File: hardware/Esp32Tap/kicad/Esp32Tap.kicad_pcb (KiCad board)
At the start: 2 copper layers, 100 x 55 mm, 53 parts, among them J1 RJ45_Console_54602-908LF, J2 RJ45_Motor_54602-908LF, J3 USB-C_HRO_TYPE-C-31-M-12, K1 G6K-2F-Y-TR DC3, Q1 S8050, SW1 KMR2-EN, SW2 KMR2-BOOT, U1 ESP32-S3-WROOM-1-N8, U2 TPS54202DDCR, U3 USBLC6-2SC6

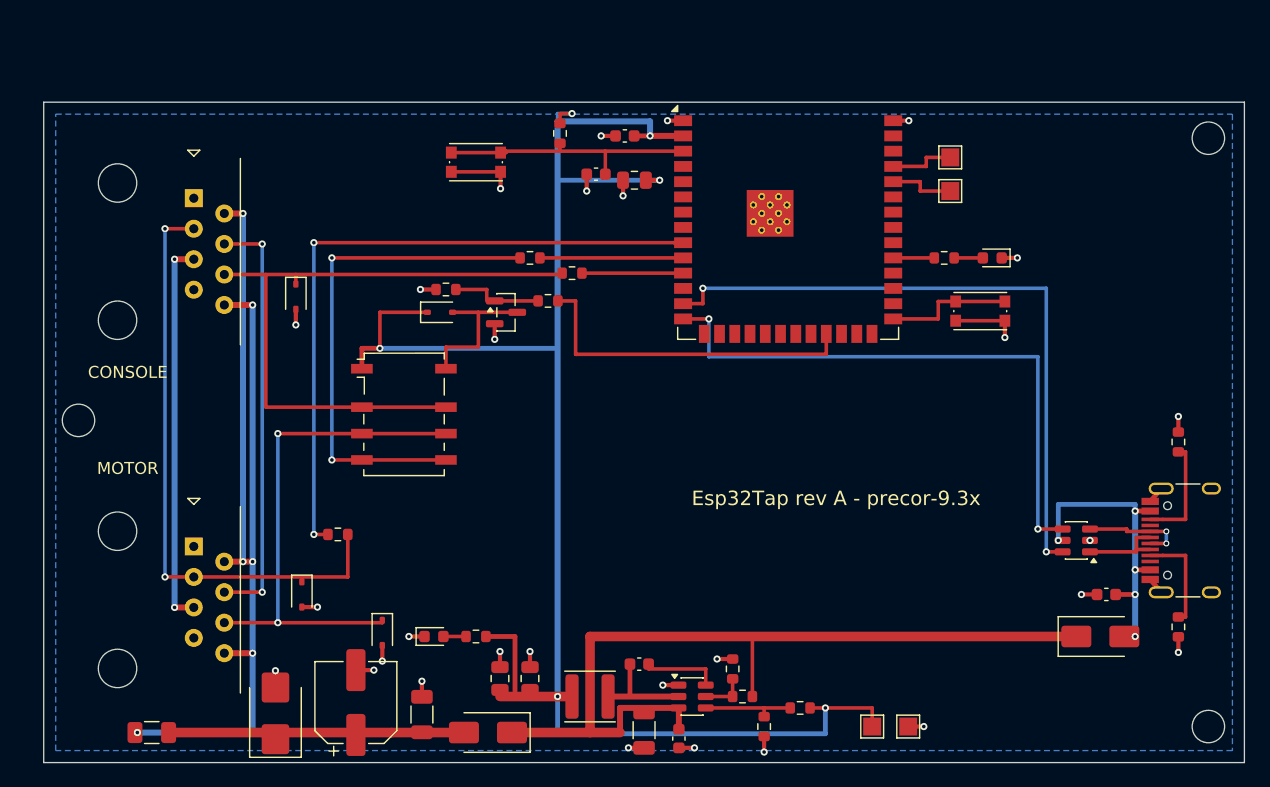
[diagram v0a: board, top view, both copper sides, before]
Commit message: hardware: generate validated Esp32Tap Rev B PCB
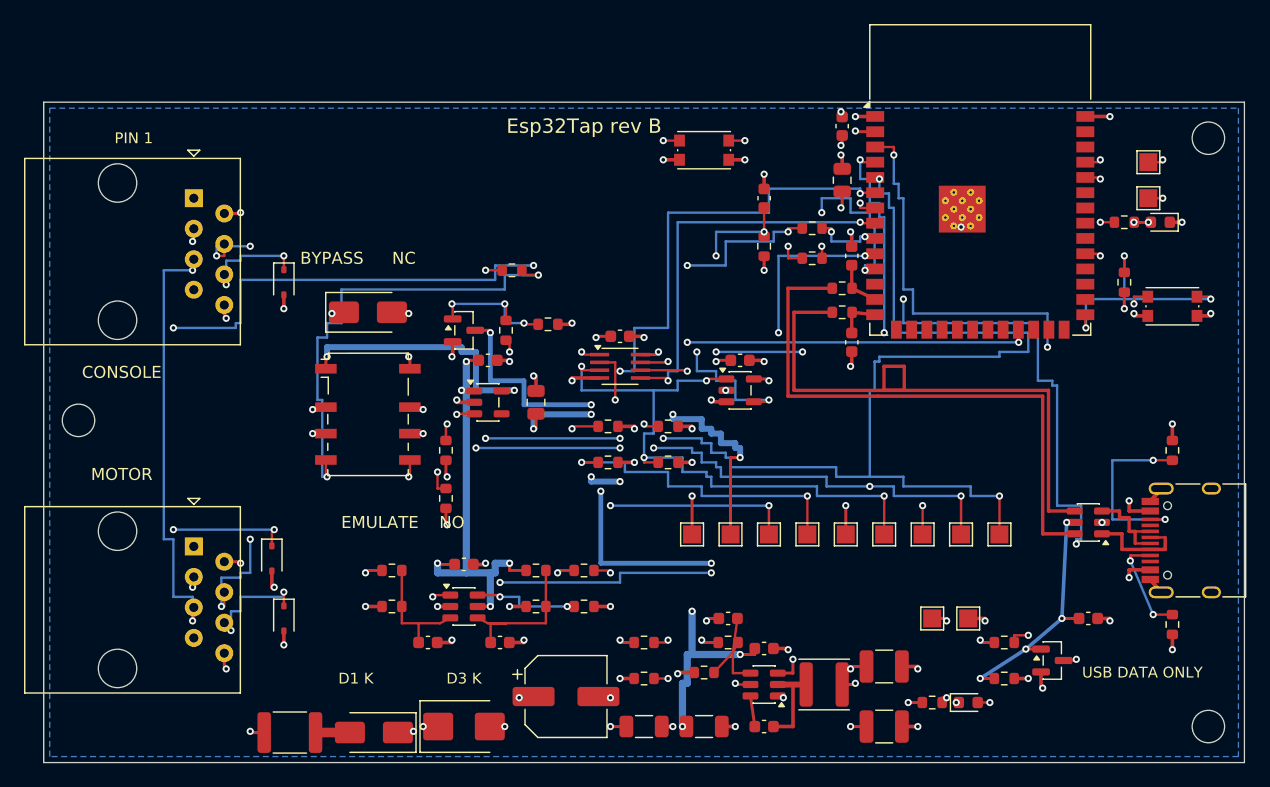
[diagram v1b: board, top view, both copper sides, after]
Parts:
- removed D2: SS34, D_SMA
- added C12: 56pF C0G 0603, Capacitor_SMD:C_0603_1608Metric, F.Cu at (157.0, 143.0)
- added C13: DNP, Capacitor_SMD:C_0603_1608Metric, F.Cu at (167.3, 112.8)
- added C14: DNP, Capacitor_SMD:C_0603_1608Metric, F.Cu at (167.3, 120.0)
- added C15: 1uF/25V X7R 0603, Capacitor_SMD:C_0603_1608Metric, F.Cu at (137.0, 121.5)
- added C16: 4.7uF/25V X7R 0805, Capacitor_SMD:C_0805_2012Metric, F.Cu at (141.0, 125.0)
- added C17: 100nF, Capacitor_SMD:C_0603_1608Metric, F.Cu at (135.0, 138.5)
- added C18: 1nF/50V C0G 0603, Capacitor_SMD:C_0603_1608Metric, F.Cu at (132.0, 145.0)
- added C19: 1nF/50V C0G 0603, Capacitor_SMD:C_0603_1608Metric, F.Cu at (138.0, 145.0)
- added C20: 100nF, Capacitor_SMD:C_0603_1608Metric, F.Cu at (148.0, 119.5)
- added C21: 100nF, Capacitor_SMD:C_0603_1608Metric, F.Cu at (158.0, 121.5)
- added Q2: 2N7002, Package_TO_SOT_SMD:SOT-23, F.Cu at (184.0, 146.5)
- added R15: 22R, Resistor_SMD:R_0603_1608Metric, F.Cu at (166.5, 115.5)
- added R16: 22R, Resistor_SMD:R_0603_1608Metric, F.Cu at (166.5, 117.5)
- added R17: 150k, Resistor_SMD:R_0603_1608Metric, F.Cu at (129.0, 139.0)
- added R18: 10k, Resistor_SMD:R_0603_1608Metric, F.Cu at (129.0, 142.0)
- added R19: 255k, Resistor_SMD:R_0603_1608Metric, F.Cu at (141.0, 139.0)
- added R20: 10k, Resistor_SMD:R_0603_1608Metric, F.Cu at (141.0, 142.0)
- added R21: 10k, Resistor_SMD:R_0603_1608Metric, F.Cu at (145.0, 139.0)
- added R22: 100k, Resistor_SMD:R_0603_1608Metric, F.Cu at (145.0, 142.0)
- added R23: 10k, Resistor_SMD:R_0603_1608Metric, F.Cu at (147.0, 127.0)
- added R24: 10k, Resistor_SMD:R_0603_1608Metric, F.Cu at (147.0, 130.0)
- added R25: 10k, Resistor_SMD:R_0603_1608Metric, F.Cu at (133.5, 129.0)
- added R26: 10k, Resistor_SMD:R_0603_1608Metric, F.Cu at (133.5, 133.0)
- added R27: 10k, Resistor_SMD:R_0603_1608Metric, F.Cu at (152.0, 127.0)
- added R28: 10k, Resistor_SMD:R_0603_1608Metric, F.Cu at (152.0, 130.0)
- added R29: 10k, Resistor_SMD:R_0603_1608Metric, F.Cu at (180.0, 148.0)
- added R30: 10k, Resistor_SMD:R_0603_1608Metric, F.Cu at (180.0, 145.0)
- added R31: 10k, Resistor_SMD:R_0603_1608Metric, F.Cu at (190.0, 115.0)
- added TP10: TX_GATE, TestPoint:TestPoint_Pad_1.5x1.5mm, F.Cu at (170.0, 136.0)
- added TP11: TX_DRV, TestPoint:TestPoint_Pad_1.5x1.5mm, F.Cu at (173.2, 136.0)
- added TP12: K1_NC_FB, TestPoint:TestPoint_Pad_1.5x1.5mm, F.Cu at (176.4, 136.0)
- added TP13: K1_NO_FB, TestPoint:TestPoint_Pad_1.5x1.5mm, F.Cu at (179.6, 136.0)
- added TP5: VIN, TestPoint:TestPoint_Pad_1.5x1.5mm, F.Cu at (154.0, 136.0)
- added TP6: +5V_RLY, TestPoint:TestPoint_Pad_1.5x1.5mm, F.Cu at (157.2, 136.0)
- added TP7: TREAD_OK, TestPoint:TestPoint_Pad_1.5x1.5mm, F.Cu at (160.4, 136.0)
- added TP8: RELAY_GATE, TestPoint:TestPoint_Pad_1.5x1.5mm, F.Cu at (163.6, 136.0)
- added TP9: RELAY_SW, TestPoint:TestPoint_Pad_1.5x1.5mm, F.Cu at (166.8, 136.0)
- added U4: TPS3700DDCR, Package_TO_SOT_SMD:SOT-23-6, F.Cu at (135.0, 142.0)
- added U5: TPS70950DBVR, Package_TO_SOT_SMD:SOT-23-5, F.Cu at (137.0, 125.0)
- added U6: SN74LVC2G08DCTR, Package_SO:SSOP-8_2.95x2.8mm_P0.65mm, F.Cu at (148.0, 122.0)
- added U7: SN74LVC1G126DBVR, Package_TO_SOT_SMD:SOT-23-5, F.Cu at (158.0, 124.0)
- C1: footprint CP_Elec_6.3x7.7 -> Capacitor_SMD:CP_Elec_6.3x7.7
- C10, C4, C5, C9: footprint C_0603_1608Metric -> Capacitor_SMD:C_0603_1608Metric
- C11: value 1uF -> 100nF; footprint C_0603_1608Metric -> Capacitor_SMD:C_0603_1608Metric
- C2, C3: value 4.7uF/50V X7R 1206 -> 10uF/25V X7R 1206; footprint C_1206_3216Metric -> Capacitor_SMD:C_1206_3216Metric
- C6, C7: value 22uF/16V 0805 -> 22uF/25V X7R 1210; footprint C_0805_2012Metric -> Capacitor_SMD:C_1210_3225Metric
- C8: footprint C_0805_2012Metric -> Capacitor_SMD:C_0805_2012Metric
- D1: footprint D_SMA -> Diode_SMD:D_SMA
- D3: value SMBJ12A -> SMBJ10A; footprint D_SMB -> Diode_SMD:D_SMB
- D4: value 1N4148WS -> SMAJ6.0CA; footprint D_SOD-323 -> Diode_SMD:D_SMA
- D5, D6, D7: footprint D_SOD-323 -> Diode_SMD:D_SOD-323
- F1: value PolyFuse 0.75A/16V 1206L075/16WR -> 1812L075/24DR; footprint Fuse_1206_3216Metric -> Fuse:Fuse_1812_4532Metric
- J1, J2: footprint RJ45_Amphenol_54602-x08_Horizontal -> Connector_RJ:RJ45_Amphenol_54602-x08_Horizontal
- J3: footprint USB_C_Receptacle_HRO_TYPE-C-31-M-12 -> Connector_USB:USB_C_Receptacle_HRO_TYPE-C-31-M-12
- K1: value G6K-2F-Y-TR DC3 -> G6K-2F-Y-TR DC5; footprint Relay_DPDT_Omron_G6K-2F-Y -> Relay_SMD:Relay_DPDT_Omron_G6K-2F-Y
- L1: footprint L_Sunlord_SWPA4030S -> Inductor_SMD:L_Sunlord_SWPA4030S
- LED1, LED2: footprint LED_0603_1608Metric -> LED_SMD:LED_0603_1608Metric
- MH1, MH2, MH3: footprint MountingHole_2.7mm_M2.5 -> MountingHole:MountingHole_2.7mm_M2.5
- Q1: value S8050 -> BC817-40,215; footprint SOT-23 -> Package_TO_SOT_SMD:SOT-23
- R1, R10, R11, R12, R13, R14, R2, R3, R4, R5, R6: footprint R_0603_1608Metric -> Resistor_SMD:R_0603_1608Metric
- R7, R8: value 4.7k -> 10k; footprint R_0603_1608Metric -> Resistor_SMD:R_0603_1608Metric
- R9: value 1k -> 560R; footprint R_0603_1608Metric -> Resistor_SMD:R_0603_1608Metric
- SW1, SW2: footprint SW_Push_1P1T_NO_CK_KMR2 -> Button_Switch_SMD:SW_Push_1P1T_NO_CK_KMR2
- TP1, TP2, TP3, TP4: footprint TestPoint_Pad_1.5x1.5mm -> TestPoint:TestPoint_Pad_1.5x1.5mm
- U1: footprint ESP32-S3-WROOM-1 -> RF_Module:ESP32-S3-WROOM-1
- U2, U3: footprint SOT-23-6 -> Package_TO_SOT_SMD:SOT-23-6
- moved R8 47.0 mm to (164.0, 110.5), turned to 0 degrees
- moved LED2 44.8 mm to (177.0, 150.0)
- moved R12 38.4 mm to (174.0, 150.0), turned to 0 degrees
- moved C7 32.2 mm to (170.0, 152.0), turned to 0 degrees
- moved C6 29.5 mm to (170.0, 147.0), turned to 0 degrees
- moved R7 20.0 mm to (164.0, 113.0)
- moved L1 19.5 mm to (165.0, 148.5), turned to 0 degrees
- moved R13 19.4 mm to (160.0, 112.0), turned to 90 degrees
- moved SW1 19.0 mm to (155.0, 104.0)
- moved C2 18.5 mm to (150.0, 152.0), turned to 0 degrees
- moved C9 18.1 mm to (166.5, 102.0), turned to 90 degrees
- moved C1 17.5 mm to (143.5, 149.5), turned to 0 degrees
- moved C8 17.3 mm to (166.5, 106.5), turned to 90 degrees
- moved TP2 16.5 mm to (192.0, 108.0)
- moved TP1 16.5 mm to (192.0, 105.0)
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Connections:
- C1 pad 1: +8V_F -> VIN
- C2 pad 1: +8V_F -> VIN
- D3 pad 1: +8V_F -> VIN
- D4 pad 1: +3V3 -> +5V_RLY
- J3 pad A8: (no net) -> unconnected-(J3-SBU1-PadA8)
- J3 pad B8: (no net) -> unconnected-(J3-SBU2-PadB8)
- K1 pad 1: +3V3 -> +5V_RLY
- K1 pad 5: TX_DRV -> K1_NO_FB
- K1 pad 6: MOT6 -> GND
- K1 pad 7: CONS6 -> K1_NC_FB
- R6 pad 1: ESP_TX -> TX_BUF
- R9 pad 1: RELAY_EN -> RELAY_GATE
- U1 pad 12: (no net) -> unconnected-(U1-IO8-Pad12)
- U1 pad 13: USB_DN_MCU -> USB_DN_R
- U1 pad 14: USB_DP_MCU -> USB_DP_R
- U1 pad 15: (no net) -> unconnected-(U1-IO3-Pad15)
- U1 pad 16: (no net) -> unconnected-(U1-IO46-Pad16)
- U1 pad 17: (no net) -> unconnected-(U1-IO9-Pad17)
- U1 pad 18: (no net) -> unconnected-(U1-IO10-Pad18)
- U1 pad 19: (no net) -> unconnected-(U1-IO11-Pad19)
- U1 pad 20: (no net) -> unconnected-(U1-IO12-Pad20)
- U1 pad 21: (no net) -> unconnected-(U1-IO13-Pad21)
- U1 pad 22: (no net) -> unconnected-(U1-IO14-Pad22)
- U1 pad 23: RELAY_EN -> RELAY_CMD
- U1 pad 24: (no net) -> unconnected-(U1-IO47-Pad24)
- U1 pad 25: (no net) -> unconnected-(U1-IO48-Pad25)
- U1 pad 26: (no net) -> unconnected-(U1-IO45-Pad26)
- U1 pad 28: (no net) -> unconnected-(U1-IO35-Pad28)
- U1 pad 29: (no net) -> unconnected-(U1-IO36-Pad29)
- U1 pad 30: (no net) -> unconnected-(U1-IO37-Pad30)
- U1 pad 32: (no net) -> unconnected-(U1-IO39-Pad32)
- U1 pad 33: (no net) -> unconnected-(U1-IO40-Pad33)
- U1 pad 34: (no net) -> unconnected-(U1-IO41-Pad34)
- U1 pad 35: (no net) -> unconnected-(U1-IO42-Pad35)
- U1 pad 38: (no net) -> unconnected-(U1-IO2-Pad38)
- U1 pad 39: (no net) -> unconnected-(U1-IO1-Pad39)
- U1 pad 4: (no net) -> K1_NC_FB
- U1 pad 5: (no net) -> K1_NO_FB
- U1 pad 6: (no net) -> TREAD_OK
- U1 pad 7: (no net) -> VBUS_PRESENT_N
- U1 pad 8: (no net) -> TX_ENABLE
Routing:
- net K1_NO_FB: track 0.00 -> 114.9 mm, vias 0 -> 7
- net TREAD_OK: track 0.00 -> 108.3 mm, vias 0 -> 10
- net K1_NC_FB: track 0.00 -> 89.8 mm, vias 0 -> 9
- net EN: track 22.0 -> 98.1 mm, vias 0 -> 8
- net +5V_RLY: track 0.00 -> 74.0 mm, vias 0 -> 9
- net RELAY_GATE: track 0.00 -> 70.5 mm, vias 0 -> 5
- net VBUS_PRESENT_N: track 0.00 -> 69.4 mm, vias 0 -> 5
- net TX_DRV: track 42.0 -> 106.5 mm, vias 2 -> 5
- net VIN: track 71.6 -> 132.3 mm, vias 0 -> 16
- net RELAY_SW: track 12.8 -> 70.5 mm, vias 0 -> 7
- net PIN3: track 50.6 -> 104.7 mm, vias 2 -> 8
- net RELAY_CMD: track 0.00 -> 53.6 mm, vias 0 -> 4
- net TX_GATE: track 0.00 -> 51.2 mm, vias 0 -> 4
- net +3V3: track 148.0 -> 198.9 mm, vias 6 -> 20
- net PIN3_RX: track 56.2 -> 6.07 mm
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- added copper zone on In1.Cu, net GND
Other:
- copper layers 2 -> 4
- board text added: "BYPASS"
- board text added: "D1 K"
- board text added: "D3 K"
- board text added: "EMULATE"
- board text added: "Esp32Tap rev B"
- board text added: "NC"
- board text added: "NO"
- board text added: "PIN 1"
- board text added: "USB DATA ONLY"
- board text removed: "Esp32Tap rev A - precor-9.3x"

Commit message: fix(hardware): tighten buck layout and reproducibility
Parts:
- moved C3 12.0 mm to (163.5, 143.5)
- moved C4 2.00 mm to (162.0, 145.5)
- moved C5 1.42 mm to (161.1, 151.1)
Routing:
- net K1_NO_FB: track 114.9 -> 121.3 mm
- net TREAD_OK: track 108.3 -> 113.1 mm, vias 10 -> 11
- net +5V_RLY: track 74.0 -> 76.4 mm
- net SW_NODE: track 8.75 -> 6.75 mm
- net VIN: track 132.3 -> 133.9 mm, vias 16 -> 15
- net BUCK_EN: track 13.1 -> 13.9 mm
- net TX_DRV: vias 5 -> 7
- net RELAY_SW: vias 7 -> 9

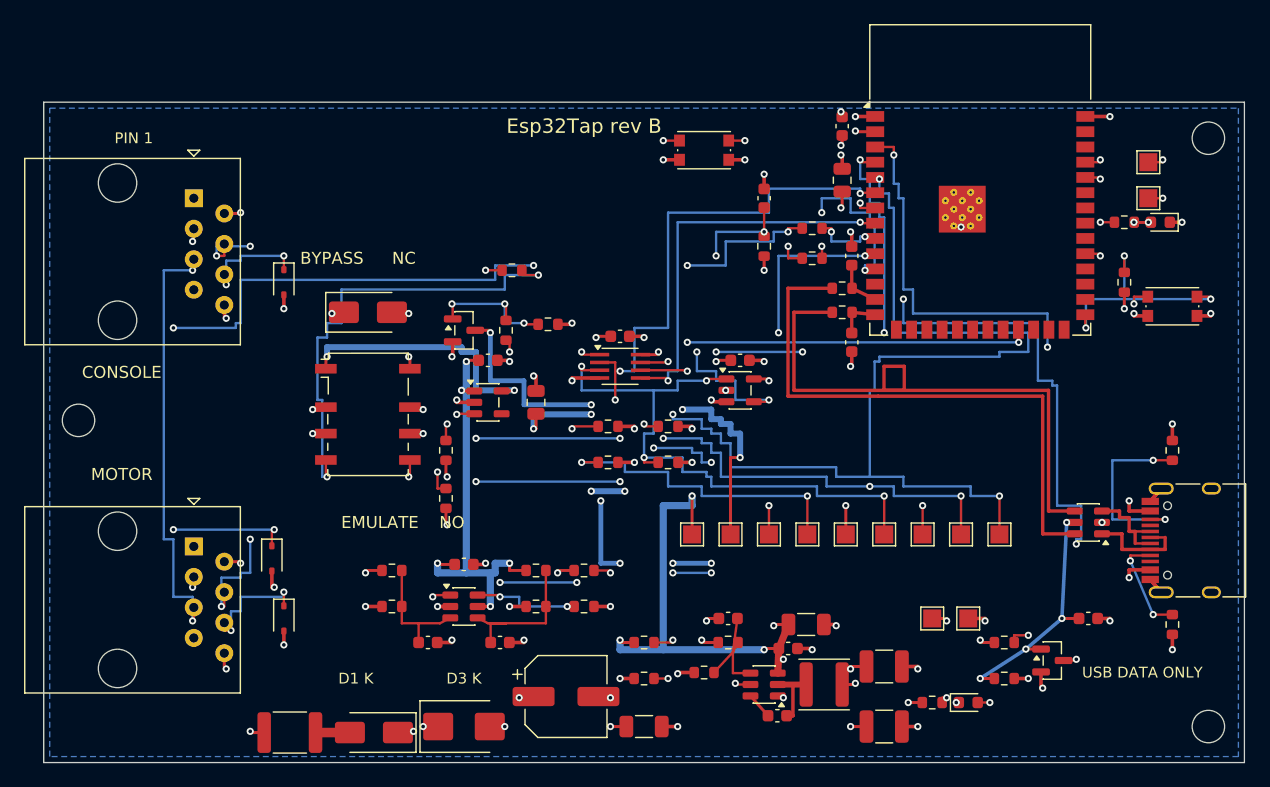
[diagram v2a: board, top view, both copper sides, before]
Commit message: hardware: clear actionable JLC DFM geometry
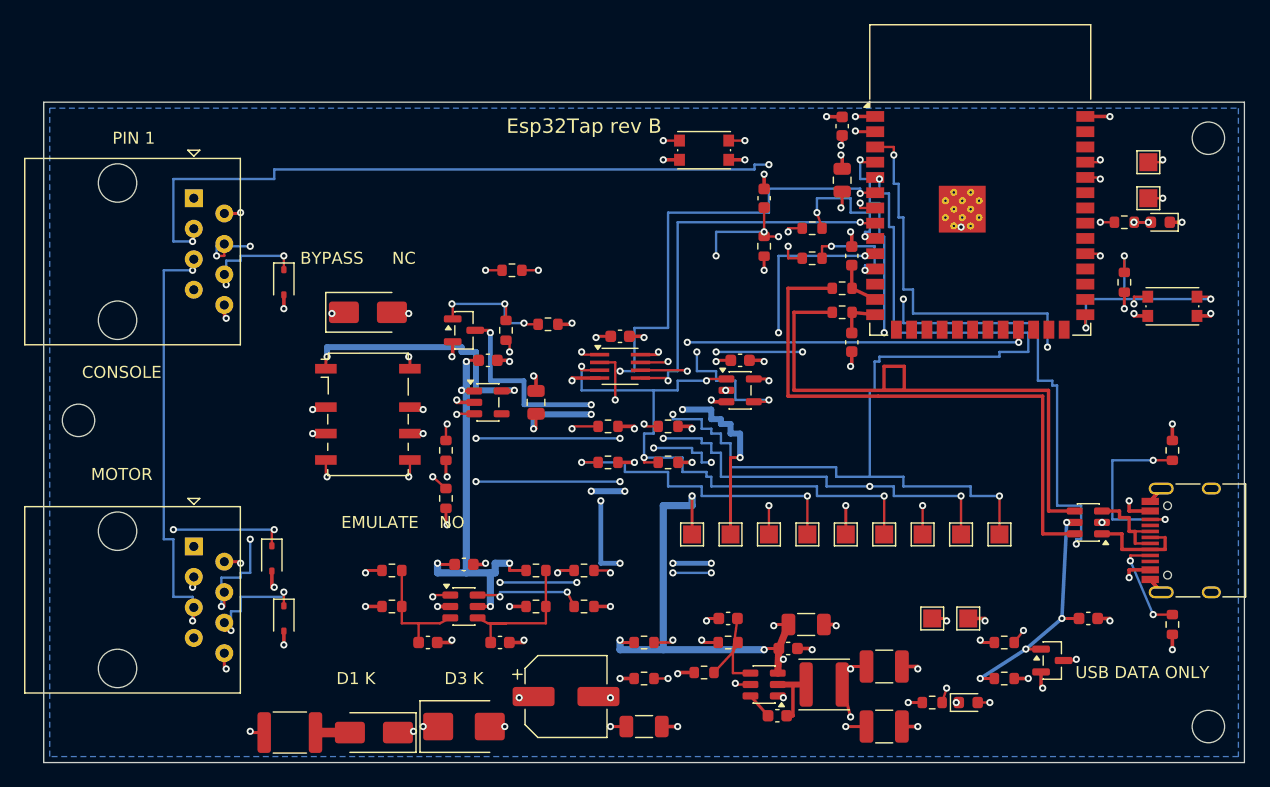
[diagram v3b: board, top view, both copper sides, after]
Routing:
- net CONS_RX: track 17.2 -> 9.13 mm, vias 3 -> 2
- net PIN3: track 104.7 -> 110.3 mm, vias 8 -> 6
- net PIN3_RX: track 6.07 -> 11.6 mm
- net EN: track 98.1 -> 100.5 mm, vias 8 -> 9
- net +3V3: track 198.9 -> 200.9 mm
- net TREAD_OK: track 113.1 -> 112.2 mm
- net GND: track 76.6 -> 77.4 mm
- net K1_NO_FB: track 121.3 -> 120.6 mm
